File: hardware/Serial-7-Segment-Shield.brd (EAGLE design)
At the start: 59.7 x 53.3 mm, 32 parts, among them J1 AVR_SPI_PRG_6PTH, U1 ARDUINO_SHIELDLABEL

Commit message: commit to QC branch
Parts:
- U1: value ARDUINO_SHIELDLABEL -> ARDUINO_R3_SHIELD; device SparkFun-Boards:DUEMILANOVE_SHIELD -> SparkFun-Boards:UNO_R3_SHIELD
- moved R14 3.62 mm to (12.0, 0.79)
- moved R15 3.15 mm to (16.0, 0.99)
- moved C4 0.61 mm to (9.50, 2.57), turned to 180 degrees
- moved R3 0.53 mm to (35.6, 46.3)
- moved R7 0.53 mm to (27.9, 46.3)
- moved R2 0.51 mm to (25.4, 46.2)
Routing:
- net VCC: track 79.6 -> 70.3 mm
- net SDA: track 45.0 -> 39.5 mm
- net RESET: track 34.7 -> 31.4 mm
- net N$5: track 9.29 -> 10.8 mm
- net N$1: track 8.99 -> 9.89 mm
- net B: track 78.2 -> 79.0 mm
- net SCL: track 47.3 -> 48.1 mm, vias 4 -> 2
- net N$17: track 3.39 -> 3.93 mm
- net N$12: track 3.39 -> 3.93 mm
- net N$11: track 3.39 -> 3.90 mm

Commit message: DESK CHANGE
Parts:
- moved R15 0.84 mm to (15.1, 1.02), turned to 0 degrees
- moved R14 0.65 mm to (11.4, 1.02)
- moved C4 0.61 mm to (9.55, 3.17)
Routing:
- net SCL: track 48.1 -> 36.4 mm
- net VCC: track 70.3 -> 79.6 mm, vias 5 -> 6
- net SDA: track 39.5 -> 46.9 mm, vias 0 -> 2
- net N$1: track 9.89 -> 9.26 mm

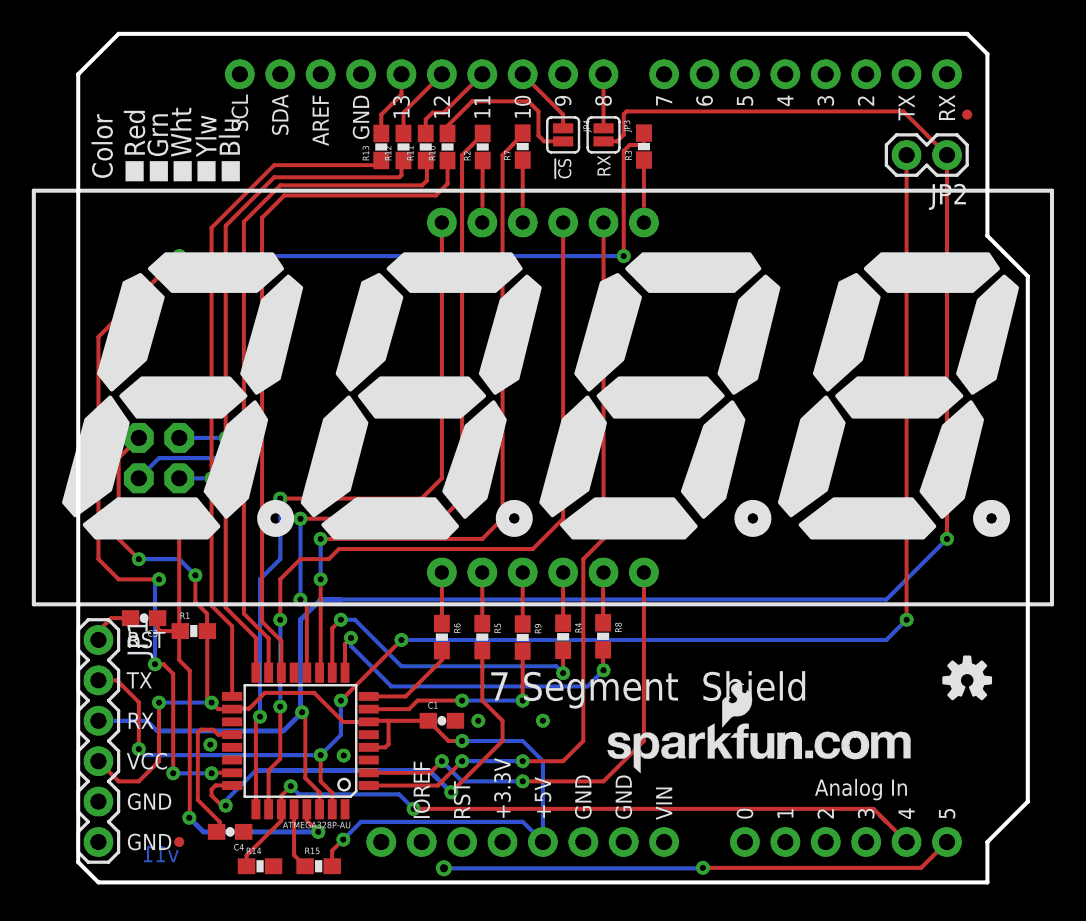
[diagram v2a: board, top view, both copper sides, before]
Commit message: Trace re-routes
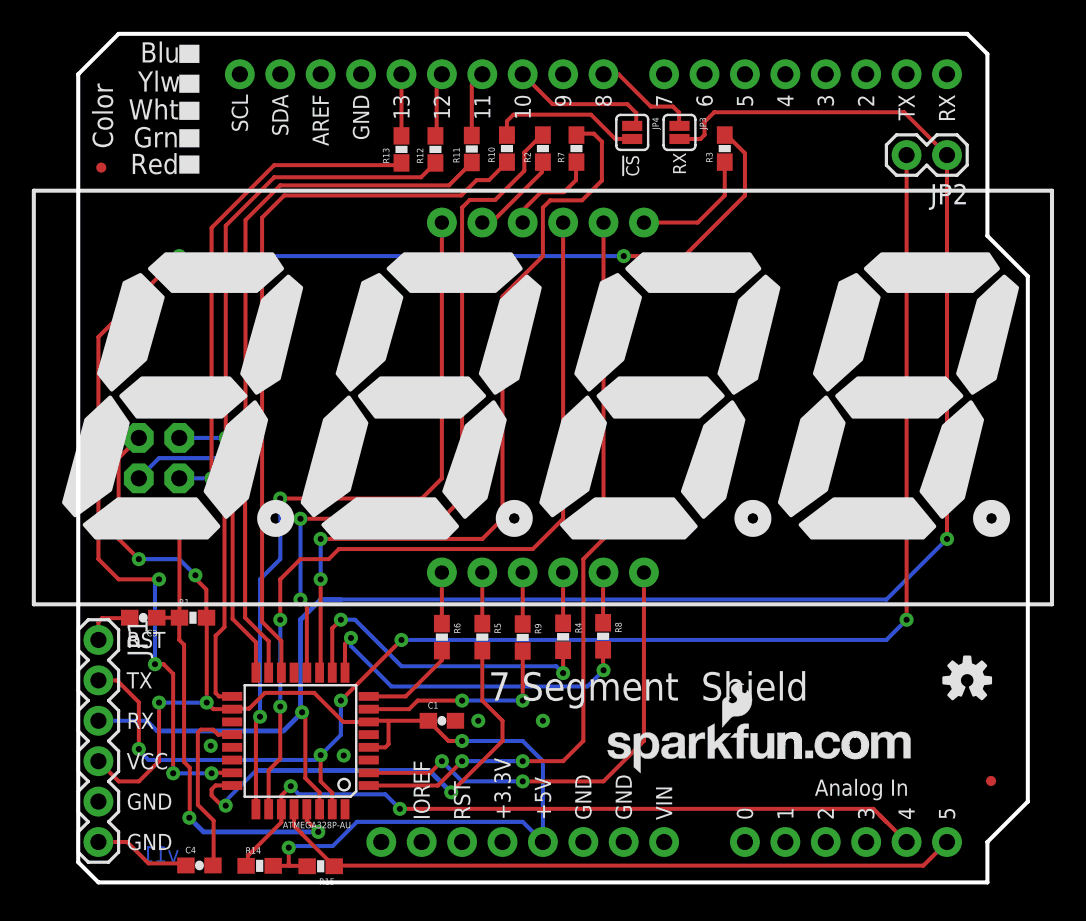
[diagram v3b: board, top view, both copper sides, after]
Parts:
- moved JP9 54.5 mm to (1.45, 44.9)
- moved JP10 51.2 mm to (57.4, 6.38)
- moved R3 5.08 mm to (40.6, 46.1)
- moved JP3 4.78 mm to (37.8, 47.1)
- moved JP4 4.35 mm to (34.8, 47.1)
- moved R2 3.79 mm to (29.2, 46.1)
- moved R10 3.74 mm to (26.9, 46.1)
- moved R7 3.38 mm to (31.3, 46.1)
- moved R11 2.90 mm to (24.7, 46.1)
- moved C4 2.86 mm to (7.62, 1.07), turned to 0 degrees
- moved R12 2.01 mm to (22.5, 46.1)
- moved R13 1.28 mm to (20.3, 46.1)
- moved R1 0.84 mm to (7.21, 16.6)
- moved R15 0.13 mm to (15.2, 1.02), turned to 180 degrees
- moved C3 0.06 mm to (4.09, 16.6)
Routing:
- net SCL: track 36.4 -> 43.8 mm, vias 2 -> 0
- net GND: track 0.00 -> 6.11 mm
- net RX: track 117.1 -> 112.0 mm
- net VCC: track 79.6 -> 84.6 mm
- net B: track 79.0 -> 83.8 mm
- net N$6: track 4.45 -> 9.06 mm
- net F: track 45.1 -> 49.7 mm
- net N$12: track 3.93 -> 7.88 mm
- net SCK: track 44.4 -> 47.7 mm
- net N$7: track 3.40 -> 6.59 mm
- net !SS: track 43.2 -> 45.9 mm
- net A: track 44.0 -> 46.5 mm
- net N$17: track 3.93 -> 6.05 mm
- net MOSI: track 50.0 -> 52.0 mm
- net N$11: track 3.90 -> 5.79 mm
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
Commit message: changed micro fid to regular
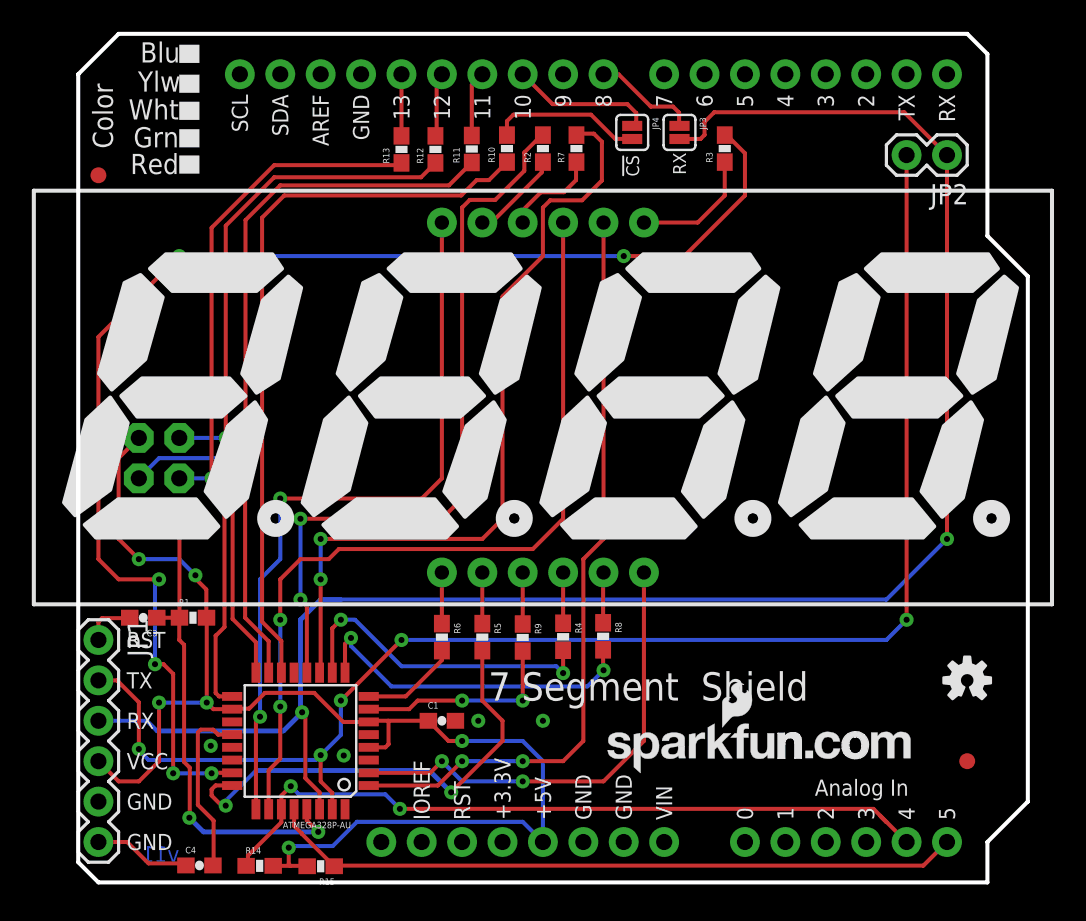
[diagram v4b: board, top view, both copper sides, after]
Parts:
- removed JP10, JP9: FIDUCIALUFIDUCIAL, SparkFun:MICRO-FIDUCIAL
- added FID1, FID2: FIDUCIAL1X2, SparkFun-Aesthetics:FIDUCIAL-1X2
